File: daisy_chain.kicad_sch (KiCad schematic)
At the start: 1 part, among them U1 BQ79616PAPRQ1

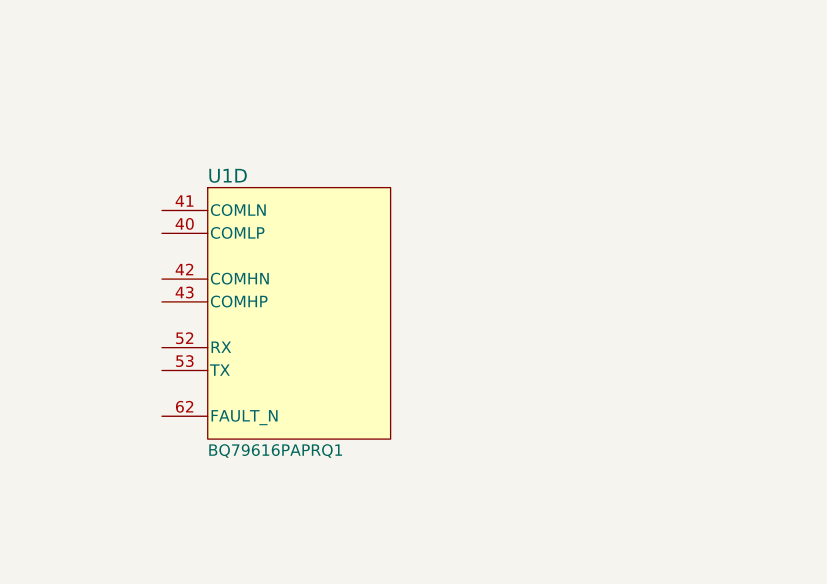
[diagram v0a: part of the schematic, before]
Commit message: SCH:[Hiarchy, Temp, Power]:Inital schmatics of temp, balance, power mostly there need to add design notes and layout notes.
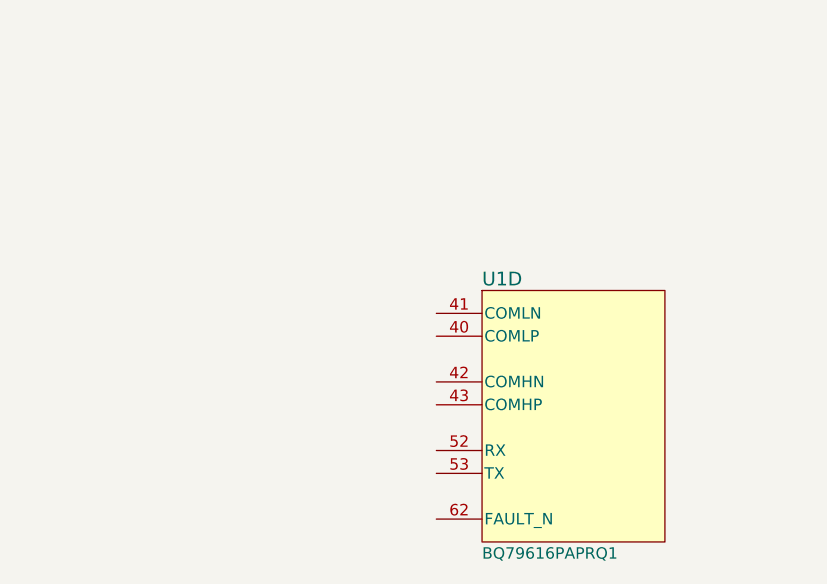
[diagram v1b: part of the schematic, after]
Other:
- moved on the sheet: U1D
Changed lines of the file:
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@@
 	(symbol
 		(lib_id "remote_bq79616paprq1:BQ79616PAPRQ1")
-		(at 121.92 67.31 0)
+		(at 152.4 78.74 0)
 		(unit 4)
 		(body_style 1)
@@
 		(dnp no)
 		(property "Reference" "U1"
-			(at 127 63.5 0)
+			(at 157.48 74.93 0)
 			(show_name no)
 			(do_not_autoplace no)
@@
 		)
 		(property "Value" "BQ79616PAPRQ1"
-			(at 127 93.98 0)
+			(at 157.48 105.41 0)
 			(show_name no)
 			(do_not_autoplace no)
@@
 		)
 		(property "Footprint" "remote_bq79616paprq1:BQ79616PAPRQ1"
-			(at 121.92 67.31 0)
+			(at 152.4 78.74 0)
 			(hide yes)
 			(show_name no)
@@
 		)
 		(property "Datasheet" "https://www.ti.com/lit/ds/symlink/bq79612-q1.pdf"
-			(at 121.92 67.31 0)
+			(at 152.4 78.74 0)
 			(hide yes)
 			(show_name no)
@@
 		)
 		(property "Description" "Battery Multi-Function Controller IC Lithium Ion 64-HTQFP (10x10)"
-			(at 121.92 67.31 0)
+			(at 152.4 78.74 0)
 			(hide yes)
 			(show_name no)
@@
 		)
 		(property "Manufacturer" "Texas Instruments"
-			(at 121.92 67.31 0)
+			(at 152.4 78.74 0)
 			(hide yes)
 			(show_name no)
@@
 		)
 		(property "Manufacturer Part Number" "BQ79616PAPRQ1"
-			(at 121.92 67.31 0)
+			(at 152.4 78.74 0)
 			(hide yes)
 			(show_name no)
@@
 		)
 		(property "Vendor" ""
-			(at 121.92 67.31 0)
+			(at 152.4 78.74 0)
 			(hide yes)
 			(show_name no)
@@
 		)
 		(property "Vendor Part Number" ""
-			(at 121.92 67.31 0)
+			(at 152.4 78.74 0)
 			(hide yes)
 			(show_name no)
@@
 		)
 		(property "Mass (g)" ""
-			(at 121.92 67.31 0)
+			(at 152.4 78.74 0)
 			(hide yes)
 			(show_name no)
@@
 		)
 		(property "RQjC (C/W)" ""
-			(at 121.92 67.31 0)
+			(at 152.4 78.74 0)
 			(hide yes)
 			(show_name no)
@@
 		)
 		(property "RQjC_top (C/W)" ""
-			(at 121.92 67.31 0)
+			(at 152.4 78.74 0)
 			(hide yes)
 			(show_name no)
@@
 		)
 		(property "Temp_max (C)" ""
-			(at 121.92 67.31 0)
+			(at 152.4 78.74 0)
 			(hide yes)
 			(show_name no)
@@
 		)
 		(property "Temp_min (C)" ""
-			(at 121.92 67.31 0)
+			(at 152.4 78.74 0)
 			(hide yes)
 			(show_name no)
@@
 		)
 		(property "Power Dissipation (W)" ""
-			(at 121.92 67.31 0)
+			(at 152.4 78.74 0)
 			(hide yes)
 			(show_name no)
@@
 		)
 		(property "Rate" ""
-			(at 121.92 67.31 0)
+			(at 152.4 78.74 0)
 			(hide yes)
 			(show_name no)
@@
 		)
 		(property "SAP Code" ""
-			(at 121.92 67.31 0)
+			(at 152.4 78.74 0)
 			(hide yes)
 			(show_name no)

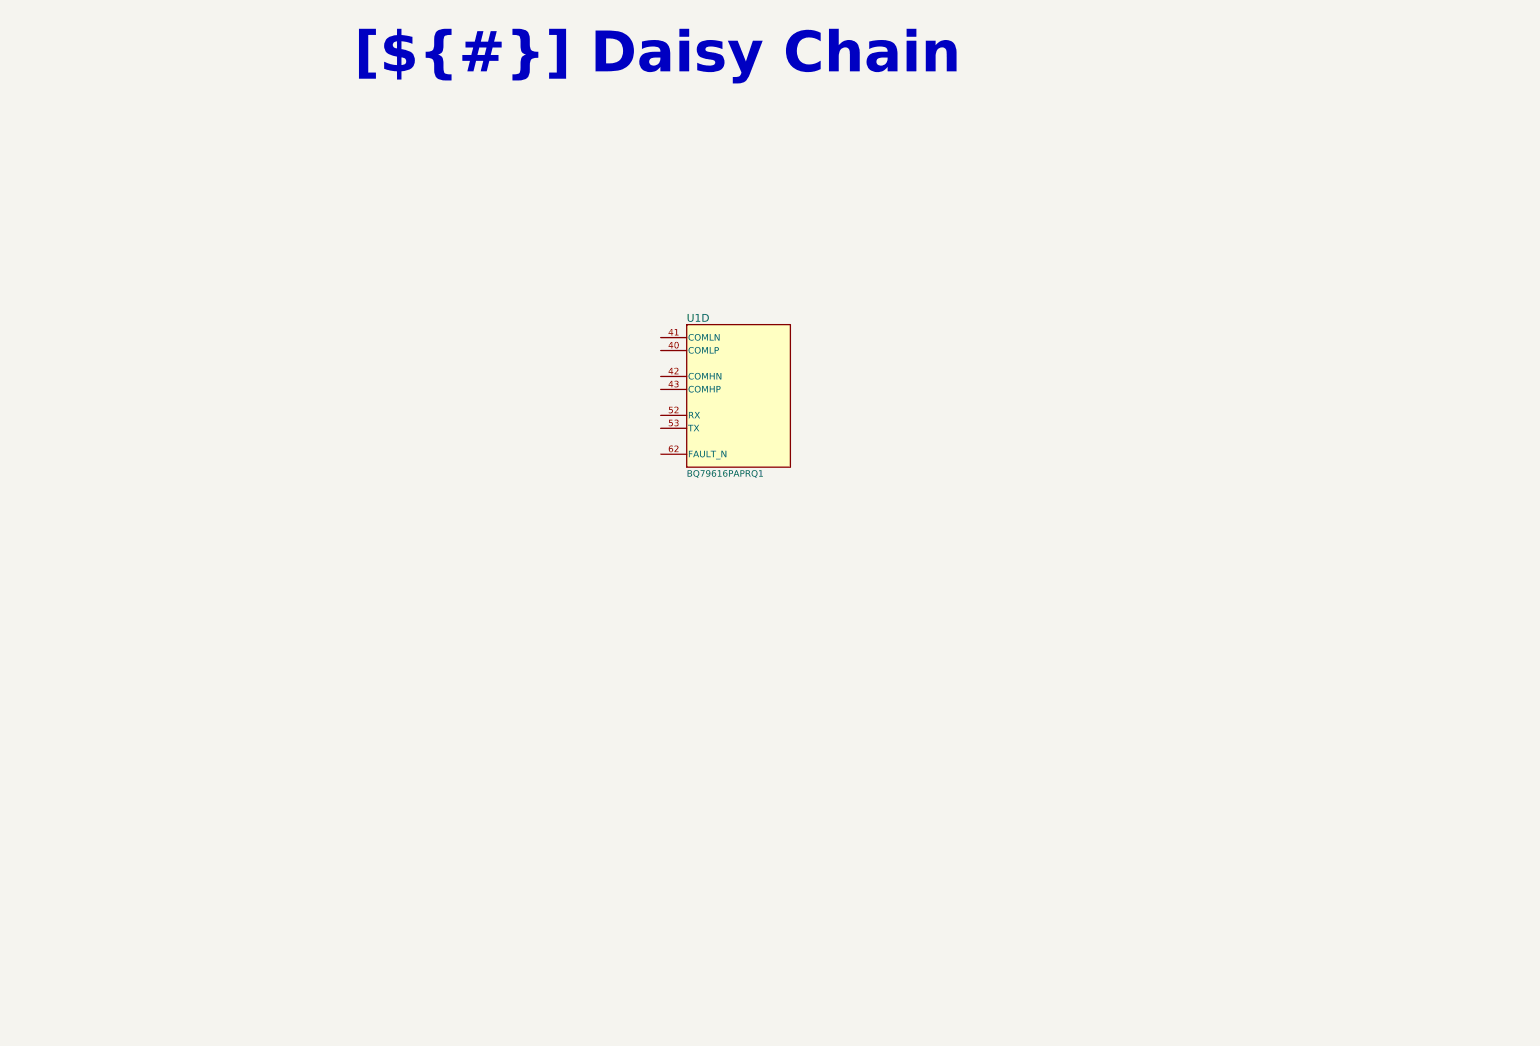
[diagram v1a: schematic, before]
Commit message: SCH: Schmatic is close to final, need to resolve a few ERC errors nothing major. Largest change will be adding seporate wires for VBAT and RefGround / Tap 0. connector position and types may change as mechaincal posision/layout is finalaized as well so holding off on layout for now.
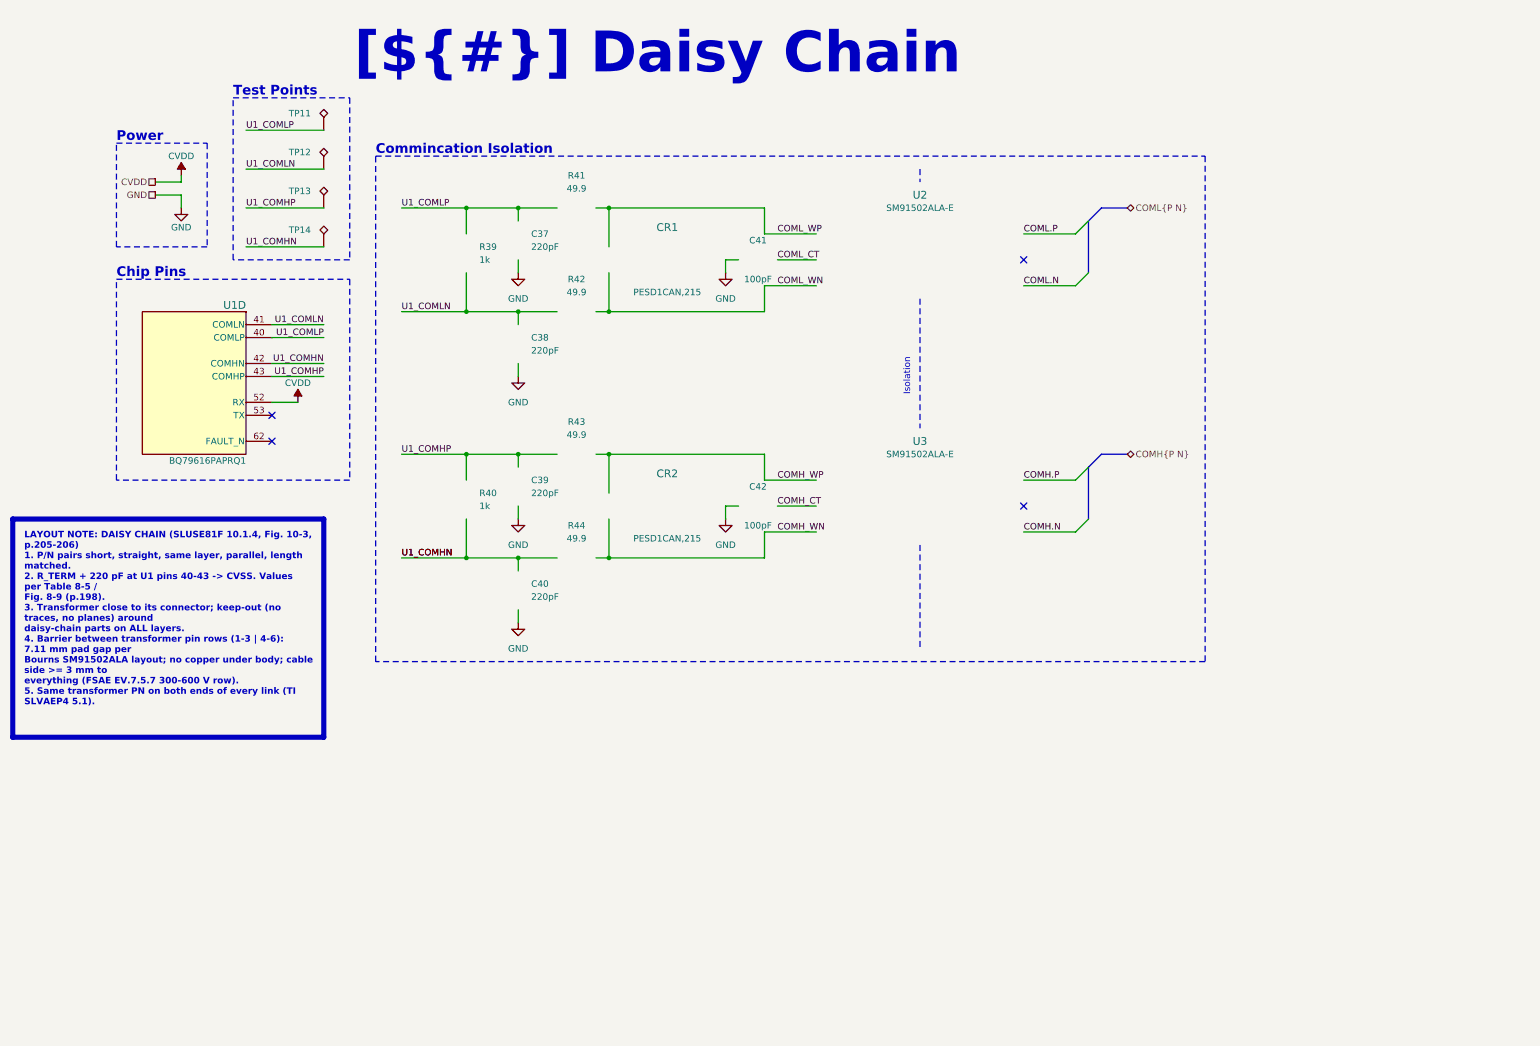
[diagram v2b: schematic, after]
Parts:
- added C37, C38, C39, C40: 220pF, remote_cl05a105ko5nnnc:C_0402_1005Metric, symbol remote_gcm1555c1h221ja16d:C
- added C41, C42: 100pF, remote_cl05a105ko5nnnc:C_0402_1005Metric, symbol remote_gcm1555c1h101ja16d:C
- added CR1, CR2: PESD1CAN,215, remote_pesd1can_215:SOT23_PESD1_NEX, symbol remote_pesd1can_215:PESD1CAN_215
- added R39, R40: 1k, remote_erj-2ge0r00x:R_0402_1005Metric, symbol remote_erj-2rkf1001x:R_US
- added R41, R42, R43, R44: 49.9, remote_erj-2ge0r00x:R_0402_1005Metric, symbol remote_crcw040249r9fked:R_US
- added TP11, TP12, TP13, TP14: (no value), TestPoint:TestPoint_Pad_D2.0mm, symbol Connector:TestPoint_Alt
- added U2, U3: SM91502ALA-E, remote_sm91502ala-e:IC6_SM91502ALA-E_BRN, symbol remote_sm91502ala-e:SM91502ALA-E
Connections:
- net U1_COMLP: now reaches U1.40 (COMLP)
- net U1_COMLP: now also C37.1, R39.1, R41.1, TP11.1
- net U1_COMLN: now reaches U1.41 (COMLN)
- net U1_COMLN: now also C38.1, R39.2, R42.1, TP12.1
- net U1_COMHN: now reaches U1.42 (COMHN)
- net U1_COMHN: now also C40.1, R40.2, R44.1, TP14.1
- net U1_COMHP: now reaches U1.43 (COMHP)
- net U1_COMHP: now also C39.1, R40.1, R43.1, TP13.1
- net CVDD: now reaches U1.52 (RX)
- new net COMH.N: U3.4
- new net COMH.P: U3.6
- new net COMH_CT: C42.1, U3.2
- new net COMH_WN: CR2.2, R44.2, U3.3
- new net COMH_WP: CR2.1, R43.2, U3.1
- new net COML.N: U2.4
- new net COML.P: U2.6
- new net COML_CT: C41.1, U2.2
- new net COML_WN: CR1.2, R42.2, U2.3
- new net COML_WP: CR1.1, R41.2, U2.1
- new net GND: C37.2, C38.2, C39.2, C40.2, C41.2, C42.2, CR1.3, CR2.3
- no-connect marks 0 -> 4
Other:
- note added: "Chip Pins"
- note added: "Commincation Isolation"
- note added: "Isolation"
- note added: "Power"
- note added: "Test Points"
- moved on the sheet: U1D

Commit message: SCH[Cleaning]:Updated Connectors not sure still, added sprate bat and ground connections, updated commincation conncetors. PCB[Layout]:Inital layout of compents need to fit on board size once tap connecton method is decided.
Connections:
- net COML_WN is gone; now on net COML_WP: CR1.2, R42.2, U2.3
- net COML.N: now also U2.6; no longer U2.4
- net COML.P: now also U2.4; no longer U2.6
- net U1_COMLN: now also C37.1, R39.1, R41.1; no longer C38.1, R39.2, R42.1
- net U1_COMLP: now also C38.1, R39.2, R42.1; no longer C37.1, R39.1, R41.1

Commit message: PCB[Routing, Silk]: Everything but led routed, need to do via stiching, and finish adding silk screen.
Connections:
- net COMH.CT: now reaches U2.5
- net COMH.CT: now also U3.5
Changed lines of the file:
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@@
 	)
 	(no_connect
-		(at 223.52 110.49)
+		(at 232.41 110.49)
 	)
 	(no_connect
-		(at 223.52 63.5)
+		(at 232.41 63.5)
 	)
 	(bus_entry
@@
 	(wire
 		(pts
+			(xy 223.52 110.49) (xy 232.41 110.49)
+		)
+		(stroke
+			(width 0)
+			(type default)
+		)
+	)
+	(wire
+		(pts
 			(xy 139.7 120.65) (xy 142.24 120.65)
 		)
@@
 		(pts
 			(xy 101.6 73.66) (xy 114.3 73.66)
+		)
+		(stroke
+			(width 0)
+			(type default)
+		)
+	)
+	(wire
+		(pts
+			(xy 223.52 63.5) (xy 232.41 63.5)
 		)
 		(stroke
@@
 			(show_name no)
 			(do_not_autoplace no)
+			(effects
+				(font
+					(size 1.27 1.27)
+					(italic yes)
+				)
+				(justify left)
+			)
+		)
+	)
+	(label "COMH.CT"
+		(at 223.52 63.5 0)
+		(fields_autoplaced yes)
+		(effects
+			(font
+				(size 1.27 1.27)
+			)
+			(justify left bottom)
+		)
+		(property "Netclass" "ISO"
+			(at 223.52 64.77 0)
+			(show_name no)
+			(do_not_autoplace no)
+			(effects
+				(font
+					(size 1.27 1.27)
+					(italic yes)
+				)
+				(justify left)
+			)
+		)
+	)
+	(label "COMH.CT"
+		(at 223.52 110.49 0)
+		(fields_autoplaced yes)
+		(effects
+			(font
+				(size 1.27 1.27)
+			)
+			(justify left bottom)
+		)
+		(property "Netclass" "ISO"
+			(at 223.52 111.76 0)
+			(show_name no)
+			(do_not_autoplace no)

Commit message: PCB[Silkscreen, DRC]: Though all drc erros minus one, not an issue just need to clear. Added silk logos
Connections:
- net COMH.CT: no longer U2.5
- net COML_WP: no longer CR1.1, R41.2, U2.1
- new net COML.CT: U2.5
- new net COML_WN: CR1.1, R41.2, U2.1
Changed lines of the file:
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@@
 		)
 	)
-	(label "COML_WP"
+	(label "COML_WN"
 		(at 175.26 105.41 0)
 		(fields_autoplaced yes)
@@
 		)
 	)
-	(label "COMH.CT"
+	(label "COML.CT"
 		(at 223.52 110.49 0)
 		(fields_autoplaced yes)
